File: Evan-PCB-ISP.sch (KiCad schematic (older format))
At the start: 14 parts

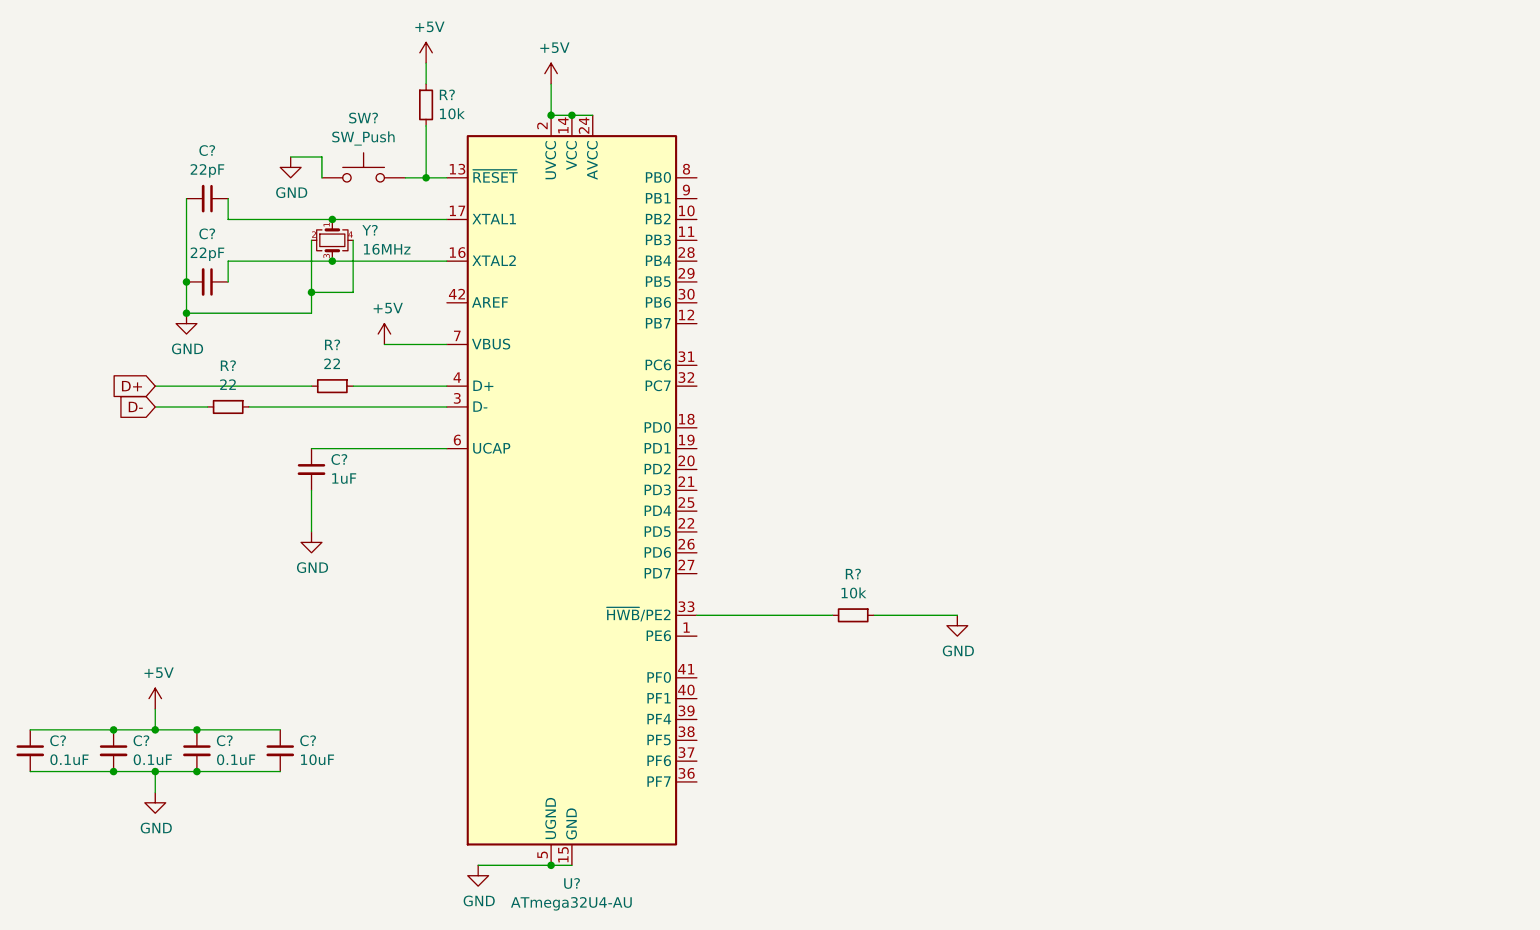
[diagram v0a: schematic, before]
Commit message: Rest of schematic & assigning footprints
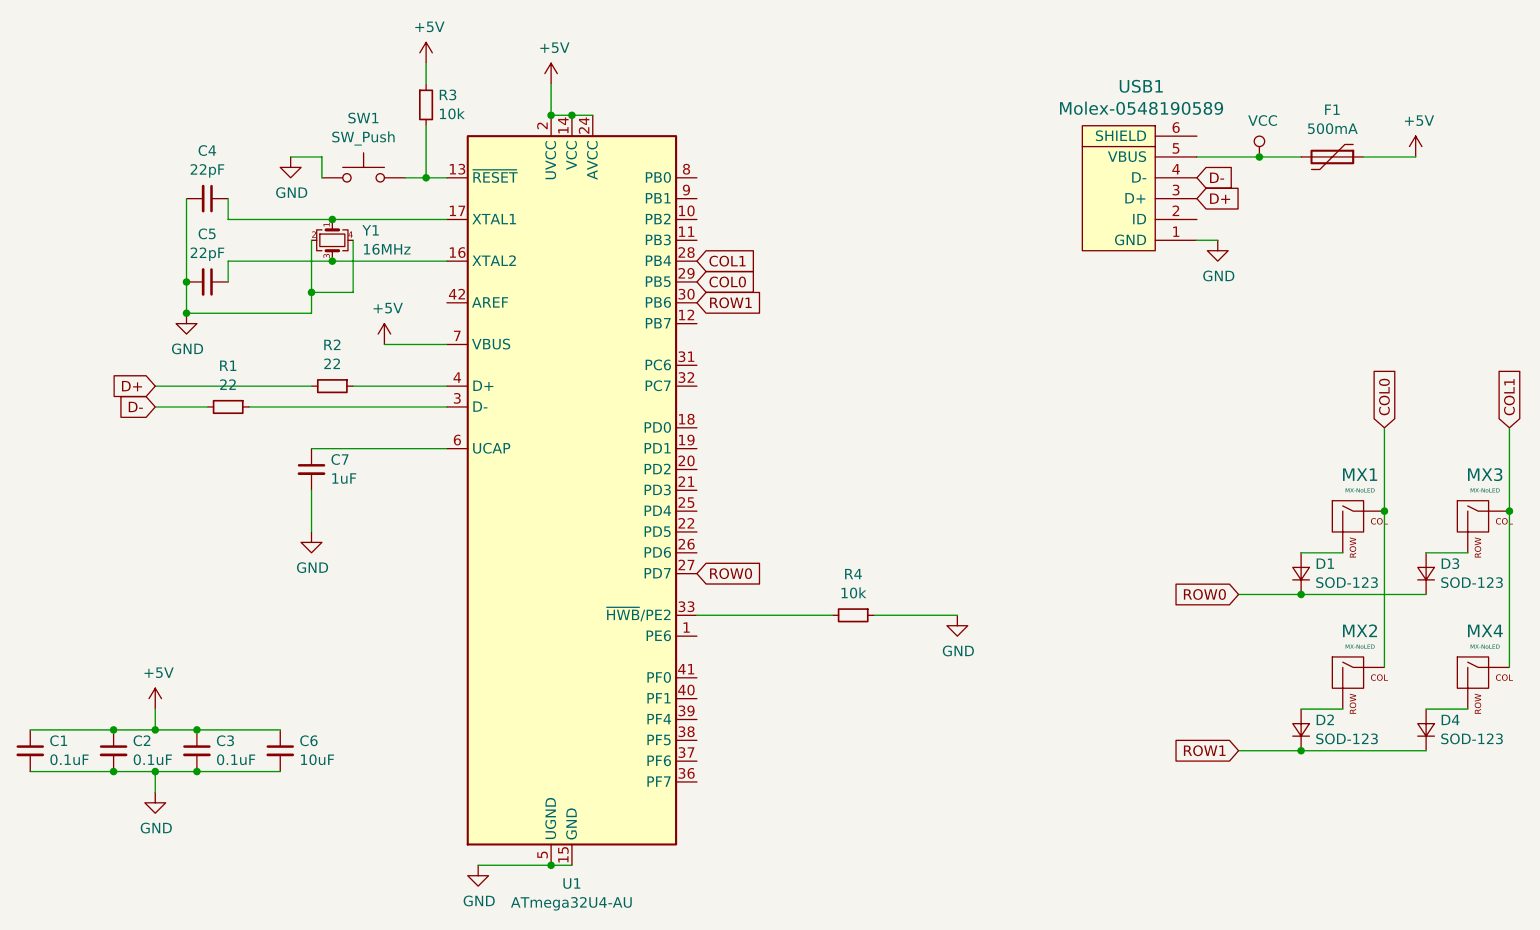
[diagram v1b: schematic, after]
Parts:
- added D1, D2, D3, D4: SOD-123, Diode_SMD:D_SOD-123, symbol Device:D_Small
- added F1: 500mA, Fuse:Fuse_1206_3216Metric, symbol Device:Polyfuse
- added MX1, MX2, MX3, MX4: MX-NoLED, MX_Alps_Hybrid:MX-1U-NoLED, symbol MX_Alps_Hybrid:MX-NoLED
- added USB1: Molex-0548190589, random-keyboard-parts:Molex-0548190589, symbol random-keyboard-parts:Molex-0548190589
- C1, C2, C3, C4, C5, C6, C7: renamed from C?; footprint (none) -> Capacitor_SMD:C_0805_2012Metric
- R1, R2, R3, R4: renamed from R?; footprint (none) -> Resistor_SMD:R_0805_2012Metric
- SW1: renamed from SW?; footprint (none) -> random-keyboard-parts:SKQG-1155865
- Y1: renamed from Y?; footprint (none) -> Crystal:Crystal_SMD_3225-4Pin_3.2x2.5mm
- gave numbers to parts that had none: 1
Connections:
- net +5V: now also F1.1
- net D+: now also USB1.3 (D+)
- net D-: now also USB1.4 (D-)
- net GND: now also USB1.1 (GND)
- net ROW0: now reaches U1.27 (PD7)
- net ROW0: now also D1.1 (K), D3.1 (K)
- net COL1: now reaches U1.28 (PB4)
- net COL1: now also MX3.1 (COL), MX4.1 (COL)
- net COL0: now reaches U1.29 (PB5)
- net COL0: now also MX1.1 (COL), MX2.1 (COL)
- net ROW1: now reaches U1.30 (PB6)
- net ROW1: now also D2.1 (K), D4.1 (K)
- new net: D1.2 (A), MX1.2 (ROW)
- new net: D3.2 (A), MX3.2 (ROW)
- new net: D2.2 (A), MX2.2 (ROW)
- new net: D4.2 (A), MX4.2 (ROW)
- new net VCC: F1.2, USB1.5 (VBUS)
